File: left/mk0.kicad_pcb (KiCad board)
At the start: 2 copper layers, 172.8 x 119.2 mm, 94 parts, among them J1 USB_C_Receptacle_USB2.0_16P, J2 AudioJack4, J3 Conn_ARM_JTAG_SWD_10, SW1 SW_RESET, SW10 tab, SW11 q, SW12 w, SW13 e, SW14 r, SW15 t, SW16 [, SW17 caps, SW18 a, SW19 s, SW2 SW_BOOT, SW20 d, SW21 f, SW22 g, SW23 ->, SW24 shift, SW25 z, SW26 x, SW27 c, SW28 v, SW29 b, SW3 `, SW30 custom2, SW31 ctrl, SW32 menu, SW33 alt, SW34 space, SW35 custom1, SW36 custom3, SW4 1, SW5 2, SW6 3, SW7 4, SW8 5, SW9 -, U1 LM3480-3.3, U2 STM32F072CBTx, Y1 8MHz

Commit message: Finish right halve
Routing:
- net GND: track 64.4 -> 66.4 mm, vias 11 -> 13
- net 3.3V: track 214.4 -> 213.7 mm
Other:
- board size 172.8 x 119.2 mm -> 172 x 119 mm
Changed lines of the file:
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@@
 		)
 	)
-	(gr_rect
-		(start 64.4144 51.5112)
-		(end 237.2614 170.7388)
+	(gr_line
+		(start 184 171)
+		(end 64 157)
 		(stroke
 			(width 0.05)
 			(type default)
 		)
-		(fill none)
+		(layer "Edge.Cuts")
+	)
+	(gr_line
+		(start 236 52)
+		(end 64 52.1)
+		(stroke
+			(width 0.05)
+			(type default)
+		)
+		(layer "Edge.Cuts")
+	)
+	(gr_line
+		(start 236 52)
+		(end 236 129.9)
+		(stroke
+			(width 0.05)
+			(type default)
+		)
+		(layer "Edge.Cuts")
+	)
+	(gr_line
+		(start 236 129.9)
+		(end 184 171)
+		(stroke
+			(width 0.05)
+			(type default)
+		)
+		(layer "Edge.Cuts")
+	)
+	(gr_line
+		(start 64 157)
+		(end 64 52.1)
+		(stroke
+			(width 0.05)
+			(type default)
+		)
 		(layer "Edge.Cuts")
 	)
@@
 	)
 	(segment
-		(start 235.4326 81.4103)
-		(end 235.4326 88.9674)
+		(start 235.1 81.0777)
+		(end 235.1 88.5124)
 		(width 0.381)
 		(layer "F.Cu")
@@
 	)
 	(segment
-		(start 235.4326 81.4103)
-		(end 232.6386 78.6163)
-		(width 0.381)
-		(layer "F.Cu")
-		(net 1)
-	)
-	(segment
 		(start 211.889975 73.9633)
 		(end 211.911475 73.9848)
@@
 	)
 	(segment
+		(start 235.1 88.5124)
+		(end 233.9086 89.7038)
+		(width 0.381)
+		(layer "F.Cu")
+		(net 1)
+	)
+	(segment
 		(start 204.9311 82.4478)
 		(end 213.330475 82.4478)
@@
 	)
 	(segment
-		(start 233.9086 89.7038)
-		(end 234.6962 89.7038)
-		(width 0.381)
-		(layer "F.Cu")
-		(net 1)
-	)
-	(segment
 		(start 204.9181 97.8138)
 		(end 227.1 97.8138)
@@
 	)
 	(segment
+		(start 232.6386 78.6163)
+		(end 235.1 81.0777)
+		(width 0.381)
+		(layer "F.Cu")
+		(net 1)
+	)
+	(segment
 		(start 200.3 83.9)
 		(end 200.3 93.1957)
@@
 		(end 221.770665 85.1154)
 		(width 0.2)
-		(layer "F.Cu")
-		(net 1)
-	)
-	(segment
-		(start 235.4326 88.9674)
-		(end 234.6962 89.7038)
-		(width 0.381)
 		(layer "F.Cu")
 		(net 1)
@@
 	)
 	(via
+		(at 223.4 112.6)
+		(size 0.6)
+		(drill 0.3)
+		(layers "F.Cu" "B.Cu")
+		(net 2)
+	)
+	(via
 		(at 218.1352 67.056)
 		(size 0.6)
@@
 	(via
 		(at 206.9846 81.1784)
+		(size 0.6)
+		(drill 0.3)
+		(layers "F.Cu" "B.Cu")
+		(net 2)
+	)
+	(via
+		(at 223.5 109.5)
 		(size 0.6)
 		(drill 0.3)
@@
 	)
 	(segment
+		(start 223.4814 113.665)
+		(end 223.4814 112.6814)
+		(width 0.381)
+		(layer "B.Cu")
+		(net 2)
+	)
+	(segment
+		(start 223.4814 109.4814)
+		(end 223.5 109.5)
+		(width 0.381)
+		(layer "B.Cu")
+		(net 2)
+	)
+	(segment
 		(start 223.4814 98.425)
 		(end 226.0061 98.425)
 		(width 0.381)
 		(layer "B.Cu")
+		(net 2)
+	)
+	(segment
+		(start 223.4814 112.6814)
+		(end 223.4 112.6)
+		(width 0.381)
+		(layer "B.Cu")
+		(net 2)
+	)
+	(segment
+		(start 223.4814 108.585)
+		(end 223.4814 109.4814)
+		(width 0.381)
+		(layer "B.Cu")

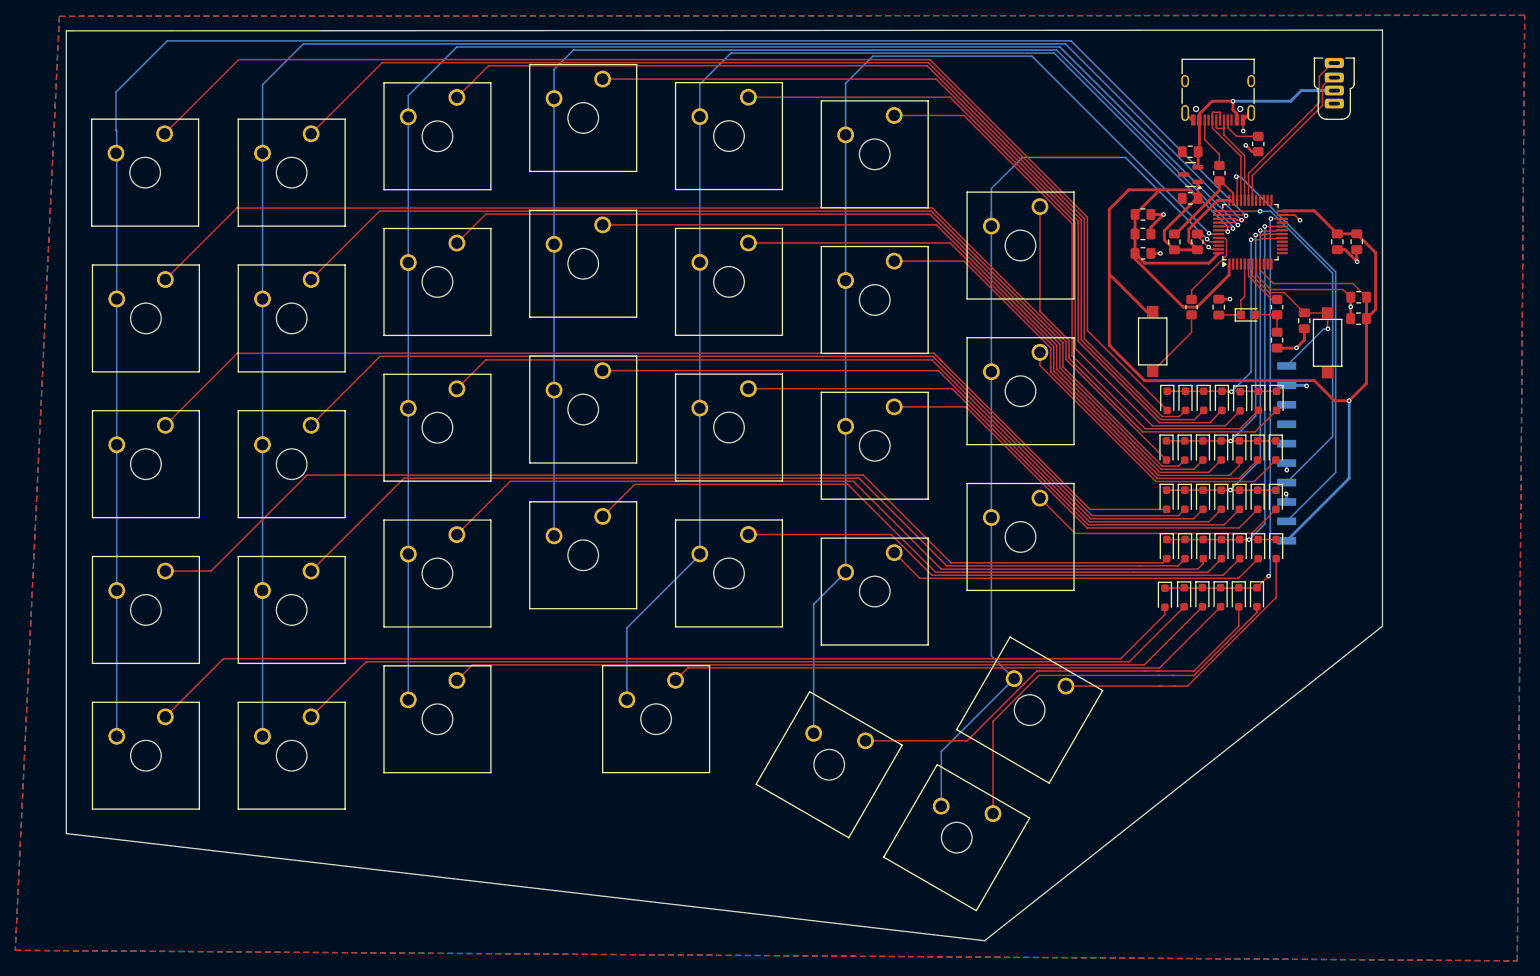
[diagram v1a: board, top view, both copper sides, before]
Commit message: left halve plate holes & python script
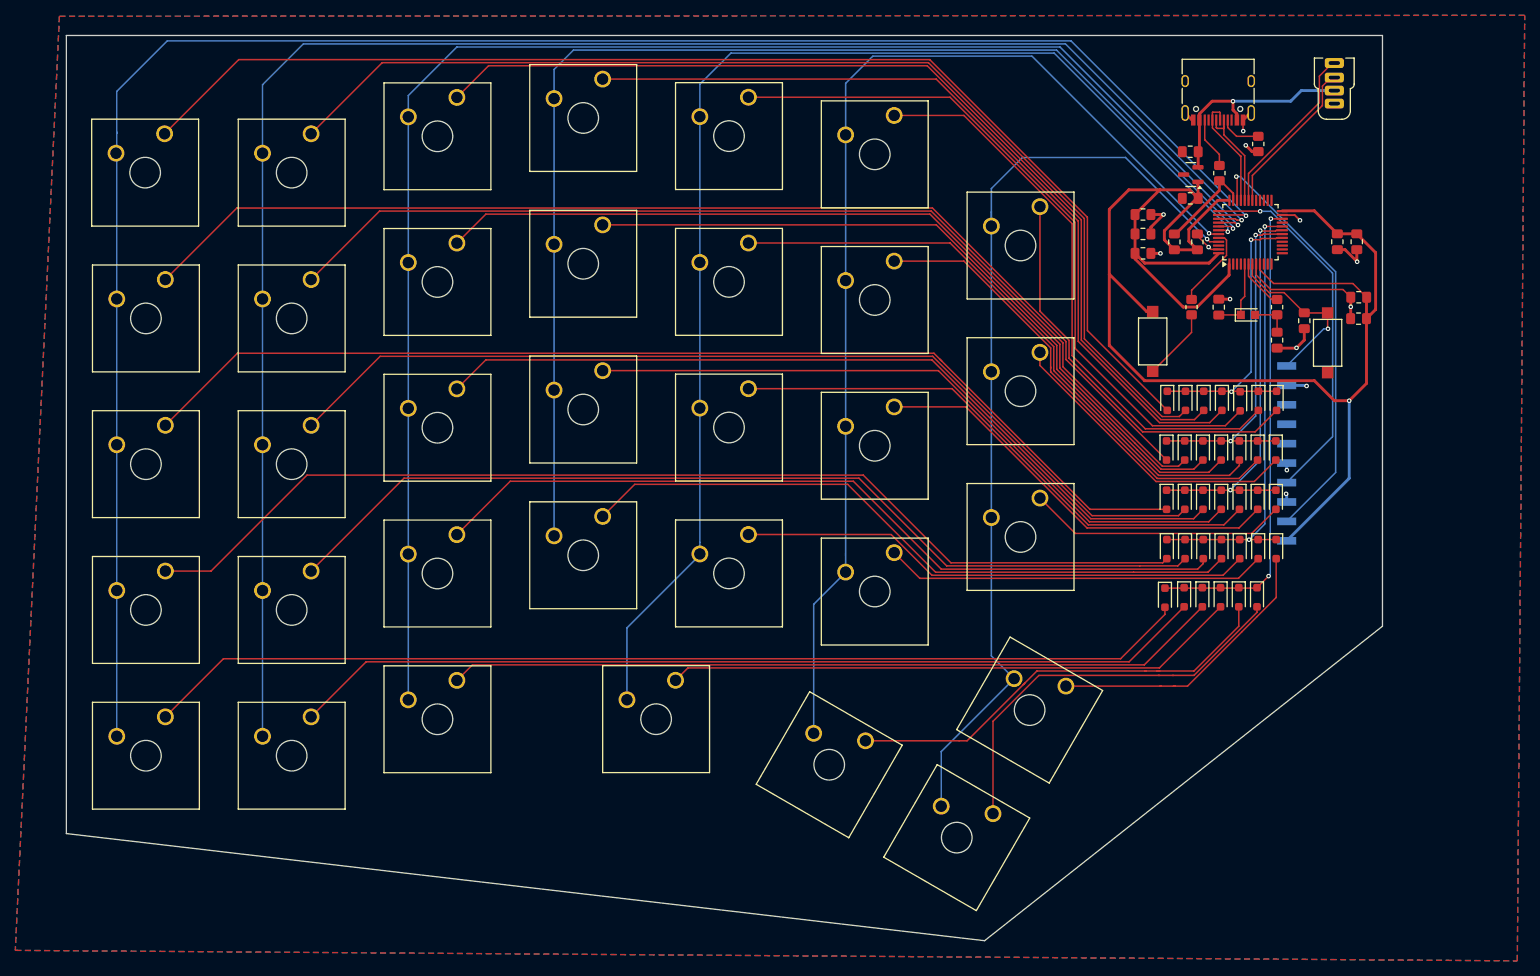
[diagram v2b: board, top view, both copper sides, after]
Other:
- board size 172 x 119 mm -> 172 x 118.3 mm

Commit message: change cristals
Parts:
- removed R4: 390, Resistor_SMD:R_0805_2012Metric_Pad1.20x1.40mm_HandSolder
- Y1: footprint Crystal:Crystal_SMD_2012-2Pin_2.0x1.2mm_HandSoldering -> Crystal:Crystal_SMD_3225-4Pin_3.2x2.5mm_HandSoldering
- moved C13 5.14 mm to (212.3, 92.8)
- moved J1 2.31 mm to (214.6, 57.4)
- moved J2 1.80 mm to (229.8, 54.5)
- moved Y1 0.52 mm to (218.1, 88.8)
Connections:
- C14 pad 1: Net-(C14-Pad1) -> Net-(U2-PF1)
- Y1 pad 2: Net-(C14-Pad1) -> GND
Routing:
- net GND: track 66.4 -> 72.0 mm
- net Net-(C14-Pad1): track 5.17 -> 0.00 mm
- net Net-(U2-PF1): track 6.59 -> 11.6 mm
- net Net-(U2-PF0): track 10.1 -> 14.2 mm
- net VBUS: track 28.6 -> 31.8 mm
- net D+: track 15.0 -> 18.0 mm
- net RX: track 22.7 -> 25.2 mm
- net TX: track 20.7 -> 23.3 mm
- net D-: track 13.9 -> 16.3 mm
- net Net-(J1-CC2): track 6.73 -> 9.02 mm
- net Net-(J1-CC1): track 6.25 -> 8.54 mm
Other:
- outline, holes or cut-outs redrawn
- board text added: "Designed in Chicago"
- board text added: "Tastiera v0.1"
